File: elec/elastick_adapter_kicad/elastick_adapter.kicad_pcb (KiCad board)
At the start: 2 copper layers, 64 x 100 mm, 19 parts, among them J1 DE-9JOYSTICK, J2 USB-C Breakout, SW1 POWER, SW2 ROTARY_SWITCH, U1 LOLIN-D32

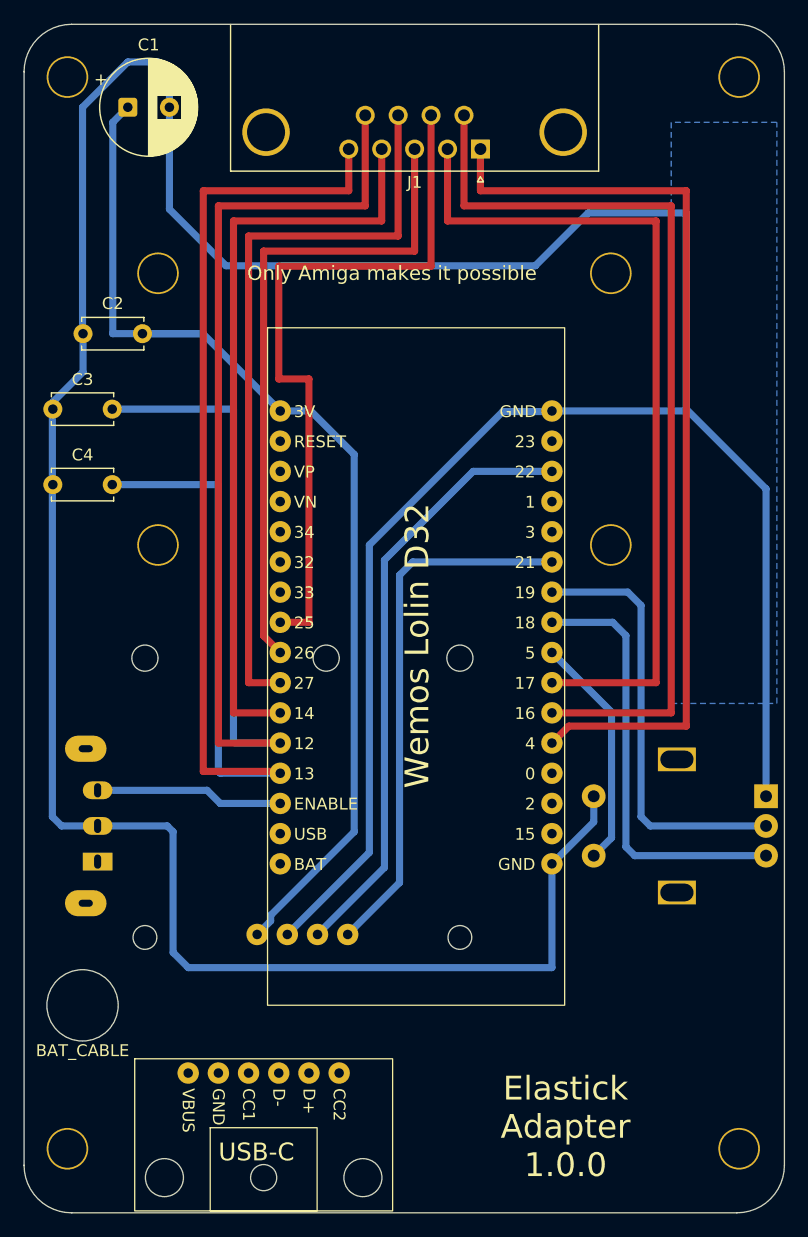
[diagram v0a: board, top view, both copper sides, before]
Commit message: make pcb more compact (+ removed usb-c adapter)
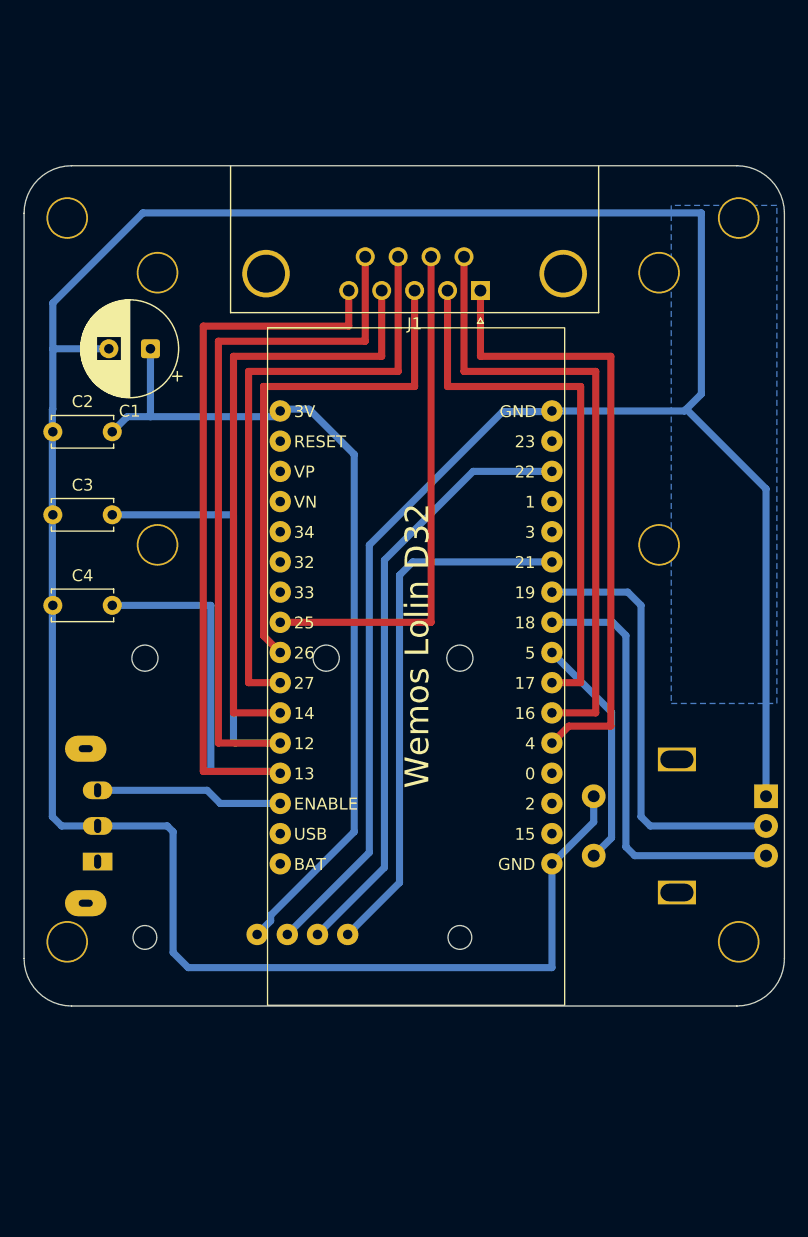
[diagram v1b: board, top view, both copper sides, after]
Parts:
- removed BAT_CABLE: battery_cable_hole, elastick:battery_cable_hole
- removed J2: USB-C Breakout, elastick:usbc
- moved C1 20.4 mm to (116.2, 88.9), turned to 180 degrees
- moved J1 11.9 mm to (144.0, 84.0)
- moved C4 10.2 mm to (108.0, 110.5)
- moved C3 8.89 mm to (108.0, 102.9)
- moved C2 8.64 mm to (113.0, 95.9)
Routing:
- net Net-(U1-16): track 77.8 -> 53.1 mm
- net Net-(U1-4): track 77.8 -> 53.2 mm
- net Net-(U1-17): track 71.2 -> 46.6 mm
- net /GND_NET: track 316.8 -> 294.2 mm
- net Net-(C4-Pad2): track 109.5 -> 87.4 mm
- net Net-(DS1-vcc): track 93.1 -> 72.2 mm
- net Net-(C3-Pad2): track 112.5 -> 91.7 mm
- net Net-(U1-25): track 60.4 -> 43.4 mm
- net Net-(U1-27): track 63.0 -> 51.1 mm
- net Net-(U1-14): track 63.8 -> 51.9 mm
- net Net-(U1-26): track 55.6 -> 43.8 mm
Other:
- board size 64 x 100 mm -> 64 x 70.7 mm
- board text added: "Elastick Adapter 1.1.0"
- board text added: "https://github.com/smart-fun/elastick"
- board text removed: "Elastick Adapter 1.0.0"
- board text removed: "Greetings to: Acclaim Accolade Activision Bethesda Softworks Blue Byte Brøderbund Capcom Cinemaware Cobra Soft Codemasters Delphine Software Electronic Arts Elite Epyx ERE Informatique Exxos Hudson Soft Imagine Infogrames Irem Kalisto Konami Lankhor Loriciels Lucas Arts Microïds MicroProse Midway Mindscape Namco NovaLogic Ocean Psygnosis Rainbird Rainbow Arts SCi Sierra SNK subLOGIC Team 17 The B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"
- board text removed: "Only Amiga makes it possible"
- board text removed: "TO THE FUTURE"
- board text removed: "TO THE PAST"
- board text removed: "⇧"

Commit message: PCB: display pin numbers for DB9
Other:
- board text added: "1"
- board text added: "2"
- board text added: "3"
- board text added: "4"
- board text added: "5"
- board text added: "6"
- board text added: "7"
- board text added: "8"
- board text added: "9"
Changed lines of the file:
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@@
 		(layer "Edge.Cuts")
+	)
+	(gr_text "5"
+		(at 132.8 85.725 180)
+		(layer "B.SilkS")
+		(effects
+			(font
+				(size 1.5 1.5)
+				(thickness 0.3)
+				(bold yes)
+			)
+			(justify bottom mirror)
+		)
+	)
+	(gr_text "9"
+		(at 134.2 77.9 180)
+		(layer "B.SilkS")
+		(effects
+			(font
+				(size 1.5 1.5)
+				(thickness 0.3)
+				(bold yes)
+			)
+			(justify bottom mirror)
+		)
+	)
+	(gr_text "8"
+		(at 137 77.9 180)
+		(layer "B.SilkS")
+		(effects
+			(font
+				(size 1.5 1.5)
+				(thickness 0.3)
+				(bold yes)
+			)
+			(justify bottom mirror)
+		)
+	)
+	(gr_text "4\n"
+		(at 135.6 85.725 180)
+		(layer "B.SilkS")
+		(effects
+			(font
+				(size 1.5 1.5)
+				(thickness 0.3)
+				(bold yes)
+			)
+			(justify bottom mirror)
+		)
 	)
 	(gr_text "design by"
@@
 				(size 1.5 1.5)
 				(thickness 0.1)
+			)
+			(justify bottom mirror)
+		)
+	)
+	(gr_text "2"
+		(at 141.2 85.725 180)
+		(layer "B.SilkS")
+		(effects
+			(font
+				(size 1.5 1.5)
+				(thickness 0.3)
+				(bold yes)
+			)
+			(justify bottom mirror)
+		)
+	)
+	(gr_text "6"
+		(at 142.6 77.9 180)
+		(layer "B.SilkS")
+		(effects
+			(font
+				(size 1.5 1.5)
+				(thickness 0.3)
+				(bold yes)
+			)
+			(justify bottom mirror)
+		)
+	)
+	(gr_text "7"
+		(at 139.8 77.9 180)
+		(layer "B.SilkS")
+		(effects
+			(font
+				(size 1.5 1.5)
+				(thickness 0.3)
+				(bold yes)
+			)
+			(justify bottom mirror)
+		)
+	)
+	(gr_text "3"
+		(at 138.4 85.725 180)
+		(layer "B.SilkS")
+		(effects
+			(font
+				(size 1.5 1.5)
+				(thickness 0.3)
+				(bold yes)
 			)
 			(justify bottom mirror)
@@
 		)
 	)
+	(gr_text "1"
+		(at 144 85.725 180)
+		(layer "B.SilkS")
+		(effects
+			(font
+				(size 1.5 1.5)
+				(thickness 0.3)
+				(bold yes)
+			)
+			(justify bottom mirror)
+		)
+	)
